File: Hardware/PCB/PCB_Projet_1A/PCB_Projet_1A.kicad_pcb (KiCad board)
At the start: 2 copper layers, 42 parts, among them J1 Conn_01x02, J10 Conn_ST_STDC14, J11 Conn_01x03, J12 Conn_01x03, J13 Conn_01x02, J14 BU33SD5WG-TR, J15 R-78B5.0-2.0, J2 Conn_01x02, J6 Conn_01x04, J7 Conn_01x04, J8 Conn_01x04, J9 Conn_01x04, U2 HC-05, U3 STM32L552CCTx

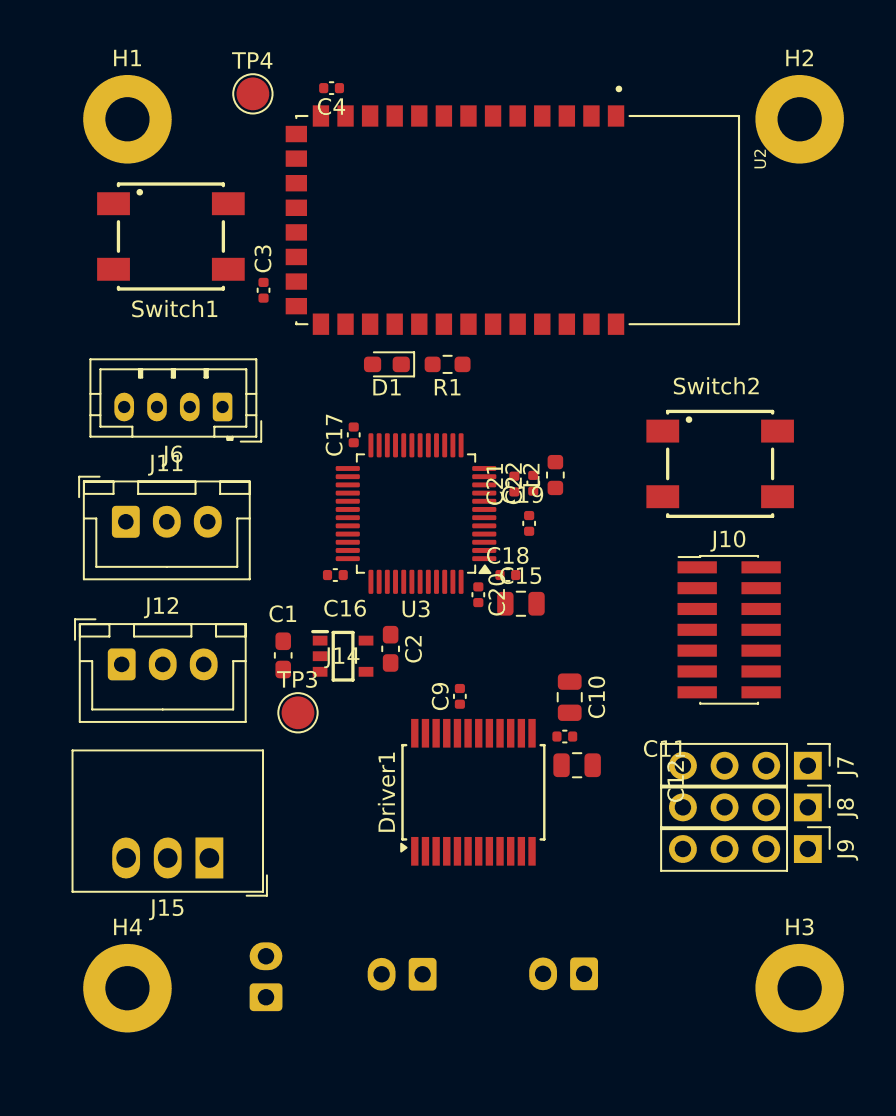
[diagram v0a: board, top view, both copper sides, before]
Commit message: Finalisation du PCB et ajout du README dans le répertoire PCB
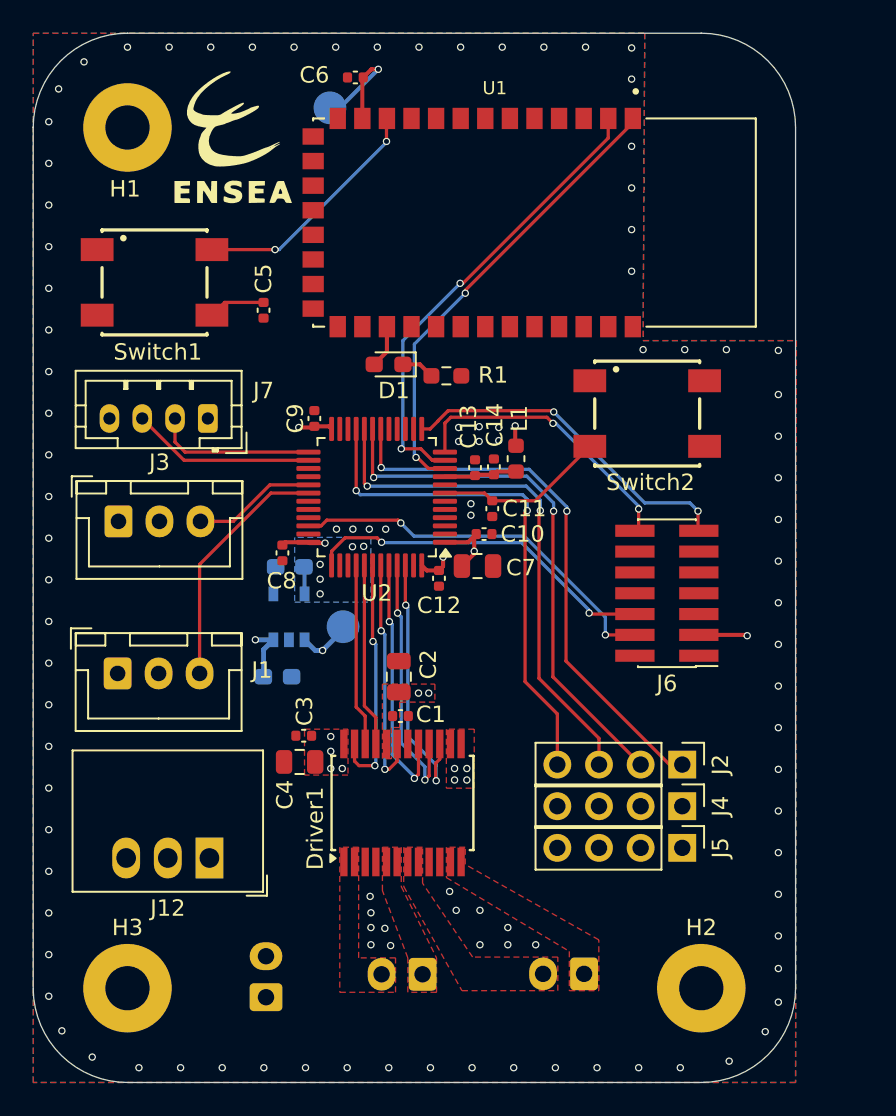
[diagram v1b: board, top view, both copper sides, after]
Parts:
- removed the H2 at (187.0, 56.0)
- added G***: LOGO, LogoEnsea:LogoEnsea, F.Cu at (152.5, 57.4)
- C15: renamed from C1; moved to B.Cu
- C16: renamed from C2; moved to B.Cu
- J11: renamed from J14; moved to B.Cu
- TP1: renamed from TP3; moved to B.Cu
- TP2: renamed from TP4; moved to B.Cu
- moved C4 16.9 mm to (156.5, 95.2), turned to 180 degrees
- moved C3 15.9 mm to (156.8, 93.6), turned to 180 degrees
- moved C2 10.5 mm to (162.6, 90.0), turned to 90 degrees
- moved J1 9.26 mm to (145.4, 89.8)
- moved J3 8.73 mm to (145.4, 80.5)
- moved C16 7.93 mm to (155.9, 83.3), turned to 180 degrees
- moved J2 7.66 mm to (179.8, 95.4)
- moved J5 7.66 mm to (179.8, 100.4)
- moved J4 7.66 mm to (179.8, 97.9)
- moved H2 6.00 mm to (181.0, 109.0)
- moved TP1 5.93 mm to (159.2, 87.0), turned to 180 degrees
- moved Switch2 5.41 mm to (177.7, 74.0)
- moved TP2 4.78 mm to (158.3, 55.3), turned to 180 degrees
- moved J6 4.41 mm to (178.9, 84.9), turned to 180 degrees
- moved Driver1 4.37 mm to (162.8, 97.7)
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- renumbered C9 to C1, C18 to C10, C19 to C11, C20 to C12, C21 to C13, C22 to C14, C10 to C2, C11 to C3, C12 to C4, C3 to C5, C4 to C6, C15 to C7, C16 to C8, C17 to C9, H3 to H2, H4 to H3, J11 to J1, J13 to J10, J15 to J12, J7 to J2, J12 to J3, J8 to J4, J9 to J5, J10 to J6, J6 to J7, J1 to J8, J2 to J9, L2 to L1, U2 to U1, U3 to U2
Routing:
- net GPIO1: track 0.00 -> 33.8 mm, vias 0 -> 2
- net GPIO2: track 0.00 -> 32.9 mm, vias 0 -> 2
- net GPIO3: track 0.00 -> 32.1 mm, vias 0 -> 2
- net GPIO4: track 0.00 -> 31.5 mm, vias 0 -> 2
- net UART4_RX: track 0.00 -> 28.4 mm, vias 0 -> 2
- net UART4_TX: track 0.00 -> 28.3 mm, vias 0 -> 2
- net +3.3V: track 0.00 -> 24.8 mm, vias 0 -> 14
- net SWDIO: track 0.00 -> 23.6 mm, vias 0 -> 2
- net SWCLK: track 0.00 -> 21.7 mm, vias 0 -> 2
- net STLINK_RX: track 0.00 -> 21.1 mm, vias 0 -> 2
- net STLINK_TX: track 0.00 -> 17.6 mm, vias 0 -> 2
- net PWMB: track 0.00 -> 16.3 mm, vias 0 -> 2
- net BIN2: track 0.00 -> 16.1 mm, vias 0 -> 2
- net BIN1: track 0.00 -> 15.8 mm, vias 0 -> 2
- net PWM_Servo2: track 0.00 -> 15.1 mm
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- added copper zone on B.Cu, net +3.3V
- added copper zone on F.Cu, net +3.3V
- added copper zone on In2.Cu, net +3.3V
- added copper zone on In2.Cu, net +5V
- added copper zone on F.Cu, net +7.5V
- added copper zone on In2.Cu, net +7.5V
- added copper zone on F.Cu, net AO1
- added copper zone on F.Cu, net AO2
- added copper zone on F.Cu, net BO1
- added copper zone on F.Cu, net BO2
- added copper zone on B.Cu, net GND
- added copper zone on F.Cu, net GND
- added copper zone on In1.Cu, net GND
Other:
- board outline added: 46.5 x 64 mm
- copper layers 2 -> 4
- board text added: "PCB Projet 1A Capodagli Janus Bui Hai Christophe Millon Raphaelle"

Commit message: amélioration PCB : vias GND
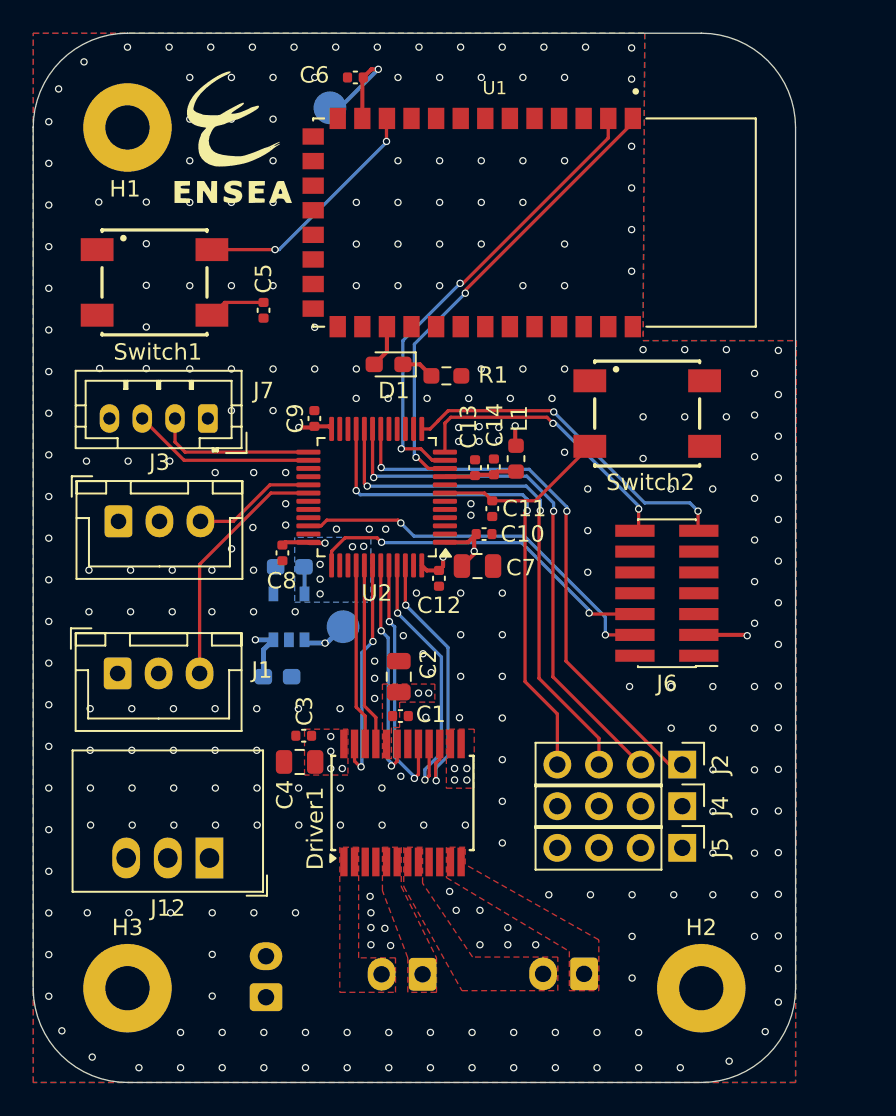
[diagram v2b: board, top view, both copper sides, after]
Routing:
- net BIN2: track 16.1 -> 16.9 mm
- net PWMB: track 16.3 -> 16.9 mm
- net PWMA: track 14.7 -> 14.2 mm
- net STBY: track 14.5 -> 14.0 mm
- net GND: vias 105 -> 299
